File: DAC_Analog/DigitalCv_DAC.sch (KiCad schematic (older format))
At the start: 14 parts

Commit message: Redo DAC_Analog
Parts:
- removed U?: ISO154x, symbol ISO154x
- removed U? (x3): TPS793xx, symbol TPS793xx
- added C? (x22): 100n, symbol C
- added C? (x3): 10n, symbol C
- added C? (x13): 10u, symbol C
- added C?: 100p, symbol C
- added C? (x2): 47u, symbol C
- added L?: BLM18AG102SN1D, symbol L_Core_Ferrite
- added R? (x4): 75, symbol R
- added R? (x9): R, symbol R
- added R?: 10k, symbol R
- added T? (x3): DA103C, symbol DA103C
- added U? (x2): TPS79333, symbol TPS793xx
- U?: value TPS793xx -> TPS79318
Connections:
- net labels added: +1.8V_rcv, +3.3V_dac, +3.3V_rcv, +5V_dac, BCK, DATA, GNDD, LRCK, MCK, Vcc
- net labels removed: +5V_anlg, GNDA
- wire segments 32 -> 278
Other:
- note added: "I2C address\n0b10011xx"
- note added: "I2C address\n0b10110xx"
- note added: "I2C address\n0b11100xx"
- moved on the sheet: C?, T?, U?

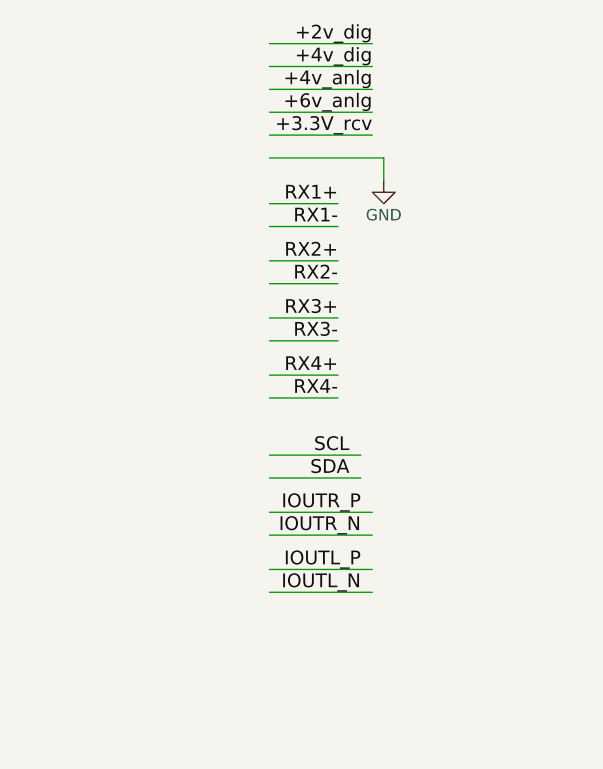
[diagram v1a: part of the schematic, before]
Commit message: Set footprints
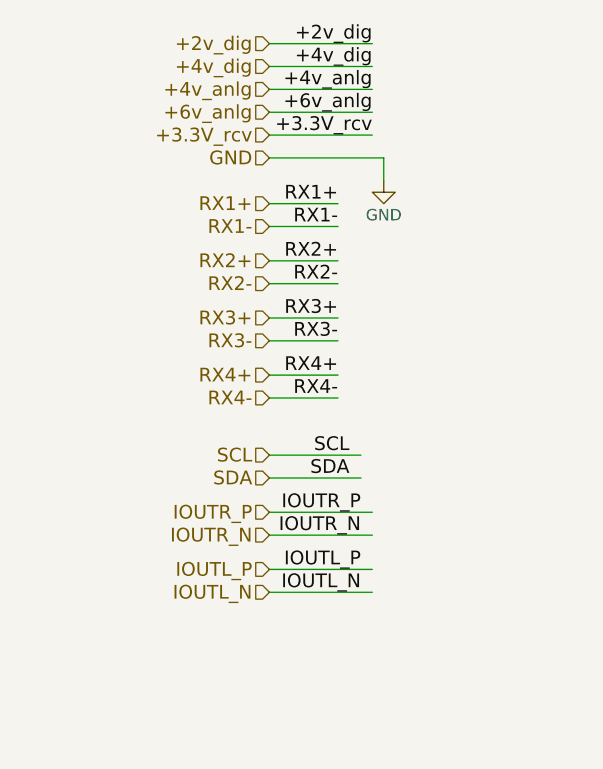
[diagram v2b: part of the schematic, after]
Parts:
- C? (x23), R? (x11): footprint (none) -> Yame_library:SM0603-MR
- C? (x14): footprint (none) -> Yame_library:SM0805-MR
- C? (x2): footprint (none) -> Yame_library:SM1206-MR
- U?: footprint (none) -> Housings_QFP:TQFP-48_7x7mm_Pitch0.5mm
- U?: footprint (none) -> Housings_SSOP:SSOP-28_5.3x10.2mm_Pitch0.65mm
- U? (x4): footprint (none) -> TO_SOT_Packages_SMD:SOT-23-5_HandSoldering
- U?: footprint (none) -> TO_SOT_Packages_SMD:SOT-223-6

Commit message: set DAC_Analog footprint
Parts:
- T? (x4): footprint (none) -> Housings_DIP:DIP-6_W10.16mm_LongPads
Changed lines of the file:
@@
 F 0 "T?" H 2300 5260 50  0000 C CNN
 F 1 "DA103C" H 2310 5170 50  0000 C CNN
-F 2 "" H 2300 4800 50  0001 C CNN
+F 2 "Housings_DIP:DIP-6_W10.16mm_LongPads" H 2300 4800 50  0001 C CNN
 F 3 "" H 2300 4800 50  0001 C CNN
 	1    2300 4800
@@
 F 0 "T?" H 2300 6160 50  0000 C CNN
 F 1 "DA103C" H 2310 6070 50  0000 C CNN
-F 2 "" H 2300 5700 50  0001 C CNN
+F 2 "Housings_DIP:DIP-6_W10.16mm_LongPads" H 2300 5700 50  0001 C CNN
 F 3 "" H 2300 5700 50  0001 C CNN
 	1    2300 5700
@@
 F 0 "T?" H 2300 7060 50  0000 C CNN
 F 1 "DA103C" H 2310 6970 50  0000 C CNN
-F 2 "" H 2300 6600 50  0001 C CNN
+F 2 "Housings_DIP:DIP-6_W10.16mm_LongPads" H 2300 6600 50  0001 C CNN
 F 3 "" H 2300 6600 50  0001 C CNN
 	1    2300 6600
@@
 F 0 "T?" H 2300 7960 50  0000 C CNN
 F 1 "DA103C" H 2310 7870 50  0000 C CNN
-F 2 "" H 2300 7500 50  0001 C CNN
+F 2 "Housings_DIP:DIP-6_W10.16mm_LongPads" H 2300 7500 50  0001 C CNN
 F 3 "" H 2300 7500 50  0001 C CNN
 	1    2300 7500

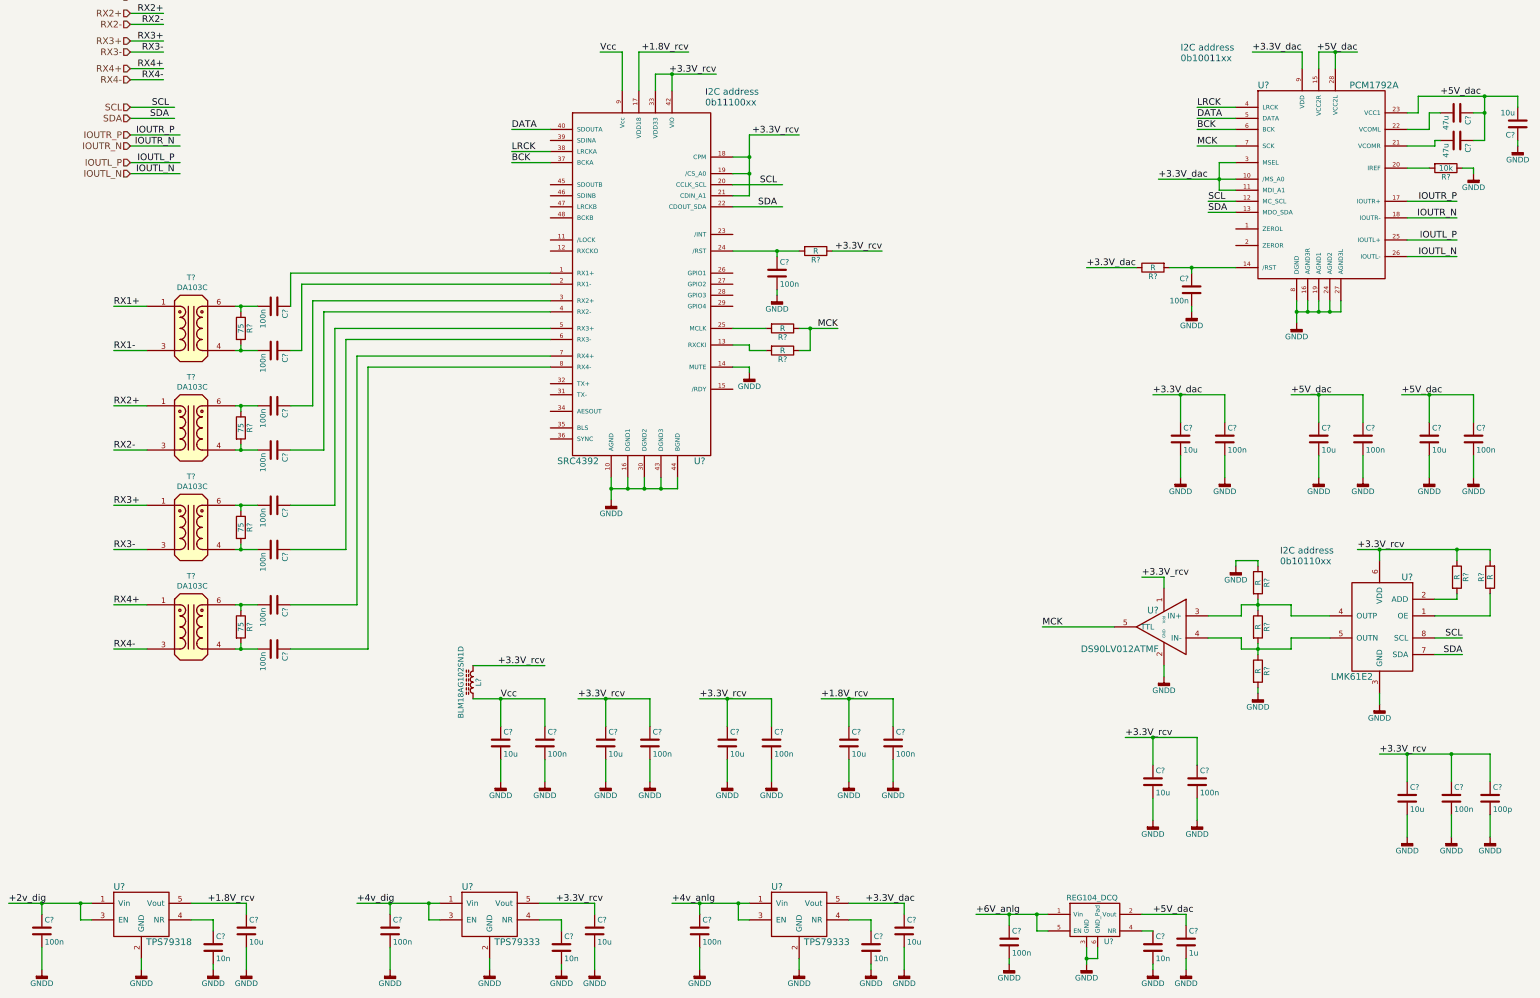
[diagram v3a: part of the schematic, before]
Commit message: Footprint assignment ok
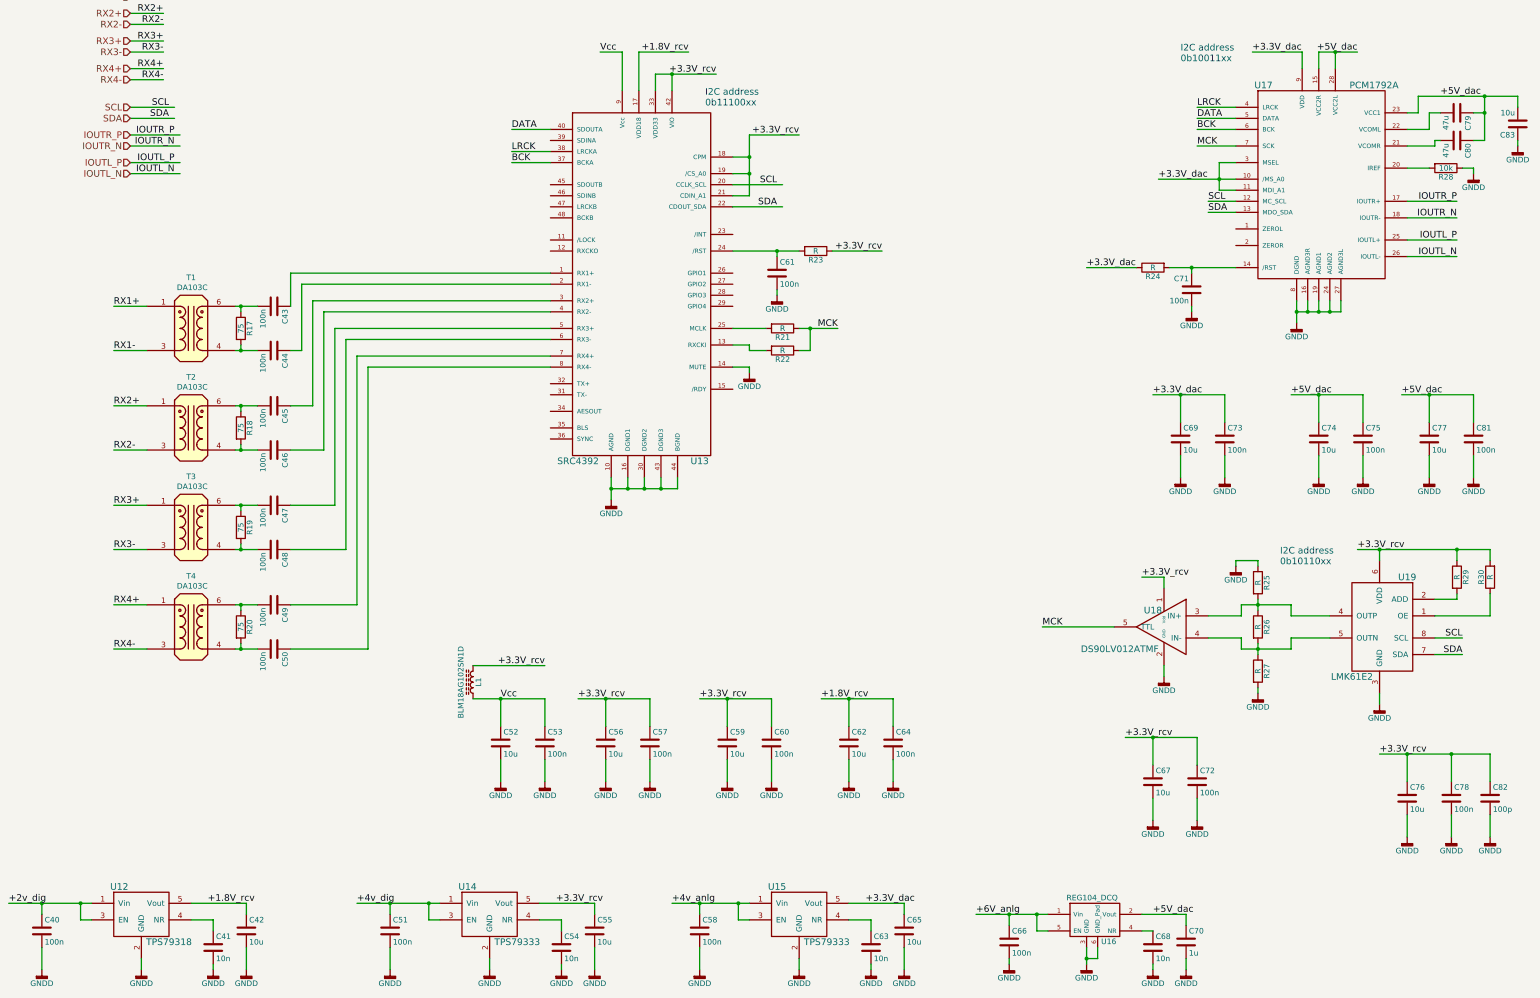
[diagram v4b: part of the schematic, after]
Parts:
- C61, C64, C73, C75, C81: renamed from C?; footprint (none) -> Yame_library:SM0603-MR
- L1: renamed from L?; footprint (none) -> Yame_library:SM0603-MR
- R21, R22, R23: renamed from R?; footprint (none) -> Yame_library:SM0603-MR
- U19: renamed from U?; footprint (none) -> Yame_library:QFM_8
- gave numbers to parts that had none: 61

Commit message: Place cmp DAC_Analog
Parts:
- added J10, J11, J12, J13: Fix, Mounting_Holes:MountingHole_3.2mm_M3, symbol Conn_01x01
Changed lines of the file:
@@
 Text HLabel 1750 1500 0    60   Input ~ 0
 GND
+$Comp
+L Conn_01x01 J10
+U 1 1 59EDF80A
+P 8650 1850
+F 0 "J10" H 8650 1950 50  0000 C CNN
+F 1 "Fix" H 8650 1750 50  0000 C CNN
+F 2 "Mounting_Holes:MountingHole_3.2mm_M3" H 8650 1850 50  0001 C CNN
+F 3 "" H 8650 1850 50  0001 C CNN
+	1    8650 1850
+	1    0    0    -1
+$EndComp
+$Comp
+L Conn_01x01 J12
+U 1 1 59EDFC7C
+P 9000 1850
+F 0 "J12" H 9000 1950 50  0000 C CNN
+F 1 "Fix" H 9000 1750 50  0000 C CNN
+F 2 "Mounting_Holes:MountingHole_3.2mm_M3" H 9000 1850 50  0001 C CNN
+F 3 "" H 9000 1850 50  0001 C CNN
+	1    9000 1850
+	1    0    0    -1
+$EndComp
+$Comp
+L Conn_01x01 J11
+U 1 1 59EDFCEF
+P 8650 2150
+F 0 "J11" H 8650 2250 50  0000 C CNN
+F 1 "Fix" H 8650 2050 50  0000 C CNN
+F 2 "Mounting_Holes:MountingHole_3.2mm_M3" H 8650 2150 50  0001 C CNN
+F 3 "" H 8650 2150 50  0001 C CNN
+	1    8650 2150
+	1    0    0    -1
+$EndComp
+$Comp
+L Conn_01x01 J13
+U 1 1 59EDFCF5
+P 9000 2150
+F 0 "J13" H 9000 2250 50  0000 C CNN
+F 1 "Fix" H 9000 2050 50  0000 C CNN
+F 2 "Mounting_Holes:MountingHole_3.2mm_M3" H 9000 2150 50  0001 C CNN
+F 3 "" H 9000 2150 50  0001 C CNN
+	1    9000 2150
+	1    0    0    -1
+$EndComp
 $EndSCHEMATC

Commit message: Update layout
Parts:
- added J14: MCLK_Test, Pin_Headers:Pin_Header_Straight_1x02_Pitch2.54mm, symbol Conn_01x02
- added R36, R37: R, Yame_library:SM0603-MR, symbol R
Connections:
- net GNDD: now also J14.2 (Pin_2)
- net MCK: now also R36.2; no longer U18.5 (TTL)
- new net: R36.1, R37.1, U18.5 (TTL)
- new net: J14.1 (Pin_1), R37.2
